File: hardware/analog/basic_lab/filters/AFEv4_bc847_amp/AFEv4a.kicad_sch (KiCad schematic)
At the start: 0 parts

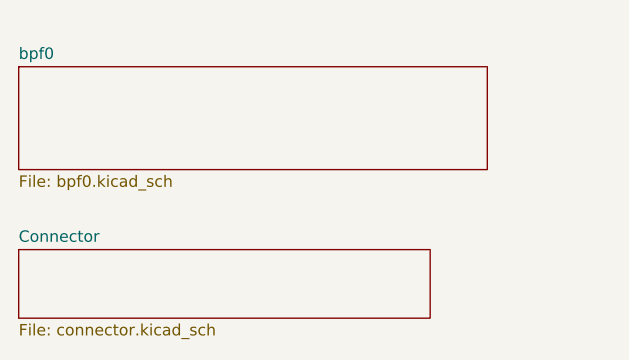
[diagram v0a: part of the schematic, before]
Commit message: started PCB LC LPF
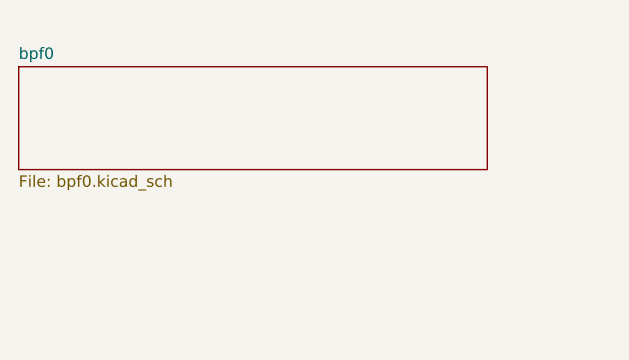
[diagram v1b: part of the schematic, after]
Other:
- removed sheet Connector
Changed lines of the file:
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@@
-    )
-  )
-  (sheet (at 21.59 73.66) (size 45.72 7.62) (fields_autoplaced)
-    (stroke (width 0.1524) (type solid) (color 0 0 0 0))
-    (fill (color 0 0 0 0.0000))
-    (property "Sheet name" "Connector" (id 0) (at 21.59 72.9484 0)
-      (effects (font (size 1.27 1.27)) (justify left bottom))
-    )
-    (property "Sheet file" "connector.kicad_sch" (id 1) (at 21.59 81.8646 0)
-      (effects (font (size 1.27 1.27)) (justify left top))
     )
   )
@@
   (sheet_instances
     (path "/" (page "1"))
-    (path "/7f528a9a-09bd-4eaa-9947-3f730f114fd1" (page "2"))
     (path "/b2b5cb11-f0cd-4899-8258-c5186877fd00" (page "3"))
     (path "/c3f60cd8-3b2b-45a1-aae3-a237e38944df" (page "4"))
@@
   )
   (symbol_instances
-    (path "/7f528a9a-09bd-4eaa-9947-3f730f114fd1/0b5a1125-8c27-4f4b-be75-954b55f47f28"
-      (reference "#PWR01") (unit 1) (value "GND") (footprint "")
-    )
-    (path "/7f528a9a-09bd-4eaa-9947-3f730f114fd1/f5f39d34-0ff3-465c-acc3-c4630fc86025"
+    (path "/c3f60cd8-3b2b-45a1-aae3-a237e38944df/03a5d1bb-eda8-4e49-8f79-de67a9f9f600"
       (reference "C1") (unit 1) (value "C") (footprint "Capacitor_SMD:C_1206_3216Metric")
     )
@@
       (reference "C2") (unit 1) (value "C") (footprint "Capacitor_SMD:C_1206_3216Metric")
     )
-    (path "/415ad690-9ea4-405f-97fc-fb5d8d9ddafd/1da5c041-d258-45eb-b4b5-98f67536845f"
-      (reference "C5") (unit 1) (value "C") (footprint "Capacitor_SMD:C_1206_3216Metric")
-    )
-    (path "/02ff8df8-9893-474d-91e8-fea3270f7696/30edc87e-b5df-4f02-801b-95b760659dc7"
-      (reference "C6") (unit 1) (value "C") (footprint "Capacitor_SMD:C_1206_3216Metric")
-    )
-    (path "/c3f60cd8-3b2b-45a1-aae3-a237e38944df/03a5d1bb-eda8-4e49-8f79-de67a9f9f600"
-      (reference "C?") (unit 1) (value "C") (footprint "Capacitor_SMD:C_1206_3216Metric")
-    )
     (path "/c3f60cd8-3b2b-45a1-aae3-a237e38944df/68c21eb8-f1e8-4f43-bbfa-9157c9321aed"
-      (reference "C?") (unit 1) (value "C") (footprint "Capacitor_SMD:C_1206_3216Metric")
+      (reference "C3") (unit 1) (value "C") (footprint "Capacitor_SMD:C_1206_3216Metric")
     )
     (path "/c3f60cd8-3b2b-45a1-aae3-a237e38944df/bb94a96f-ee19-4353-b6ff-3c42241aed6a"
-      (reference "C?") (unit 1) (value "C") (footprint "Capacitor_SMD:C_1206_3216Metric")
-    )
-    (path "/7f528a9a-09bd-4eaa-9947-3f730f114fd1/e66d98d6-e509-471c-a219-c980e6f6376f"
-      (reference "J1") (unit 1) (value "Connector_Generic_Conn_01x20") (footprint "Connector_PinHeader_2.54mm:PinHeader_1x20_P2.54mm_Vertical")
-    )
-    (path "/b2b5cb11-f0cd-4899-8258-c5186877fd00/4a702d93-95a1-453e-bdc0-0a6f50a39eb8"
-      (reference "J2") (unit 1) (value "Connector_Generic_Conn_01x02") (footprint "Connector_PinHeader_2.54mm:PinHeader_1x02_P2.54mm_Vertical")
+      (reference "C4") (unit 1) (value "C") (footprint "Capacitor_SMD:C_1206_3216Metric")
     )
     (path "/c3f60cd8-3b2b-45a1-aae3-a237e38944df/670d398b-a026-4319-88ef-354daf94f43b"
@@
     )
     (path "/c3f60cd8-3b2b-45a1-aae3-a237e38944df/1001d5ff-43e6-4b7a-912e-ae97990f49ea"
-      (reference "L?") (unit 1) (value "L") (footprint "Inductor_SMD:L_1206_3216Metric")
+      (reference "L2") (unit 1) (value "L") (footprint "Inductor_SMD:L_1206_3216Metric")
     )
     (path "/c3f60cd8-3b2b-45a1-aae3-a237e38944df/859876e6-f802-4bc8-b380-83c6f3fc43f8"
-      (reference "L?") (unit 1) (value "L") (footprint "Inductor_SMD:L_1206_3216Metric")
-    )
-    (path "/415ad690-9ea4-405f-97fc-fb5d8d9ddafd/59945e65-59ce-4200-8603-4b8d3cea220b"
-      (reference "R1") (unit 1) (value "R") (footprint "Resistor_SMD:R_1206_3216Metric")
-    )
-    (path "/415ad690-9ea4-405f-97fc-fb5d8d9ddafd/245e2d2c-1ef8-4697-a385-6ad5f05a99ae"
-      (reference "R2") (unit 1) (value "R") (footprint "Resistor_SMD:R_1206_3216Metric")
-    )
-    (path "/415ad690-9ea4-405f-97fc-fb5d8d9ddafd/9c86227d-76ba-49a2-9ffe-628fd0f6d395"
-      (reference "R3") (unit 1) (value "R") (footprint "Resistor_SMD:R_1206_3216Metric")
-    )
-    (path "/415ad690-9ea4-405f-97fc-fb5d8d9ddafd/29a058b7-613d-457b-a130-58debcf0061a"
-      (reference "R4") (unit 1) (value "R") (footprint "Resistor_SMD:R_1206_3216Metric")
-    )
-    (path "/02ff8df8-9893-474d-91e8-fea3270f7696/6bf1d94f-9a8a-4ec3-a9d8-ef69f23afcf7"
-      (reference "R5") (unit 1) (value "R") (footprint "Resistor_SMD:R_1206_3216Metric")
-    )
-    (path "/02ff8df8-9893-474d-91e8-fea3270f7696/78c48e67-8f5c-4782-9ccb-ccd410e12b6a"
-      (reference "R6") (unit 1) (value "R") (footprint "Resistor_SMD:R_1206_3216Metric")
-    )
-    (path "/02ff8df8-9893-474d-91e8-fea3270f7696/0f7f95a6-3343-49b5-8712-e2c908851fa4"
-      (reference "R7") (unit 1) (value "R") (footprint "Resistor_SMD:R_1206_3216Metric")
-    )
-    (path "/02ff8df8-9893-474d-91e8-fea3270f7696/493edbbe-c19f-441e-bdc6-d05b0ec125a6"
-      (reference "R8") (unit 1) (value "R") (footprint "Resistor_SMD:R_1206_3216Metric")
-    )
-    (path "/7f528a9a-09bd-4eaa-9947-3f730f114fd1/8cc7ff4e-c2bb-41cc-a737-5718c83f8591"
-      (reference "R9") (unit 1) (value "R") (footprint "Resistor_SMD:R_0805_2012Metric")
+      (reference "L3") (unit 1) (value "L") (footprint "Inductor_SMD:L_1206_3216Metric")
     )
   )
